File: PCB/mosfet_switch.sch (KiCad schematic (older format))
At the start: 4 parts, among them Q1 DMN1150UFB-7B, Q2 NVTR0202PLT1G

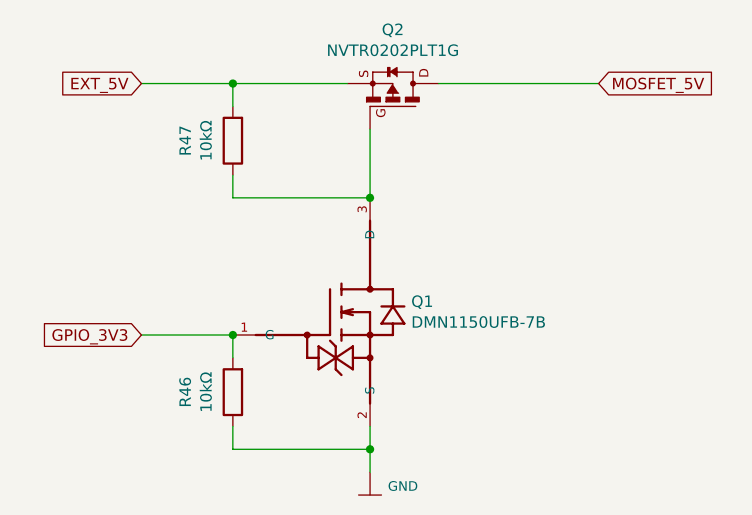
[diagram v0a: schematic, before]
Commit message: Patrick: implemented fuses and bidirectional security diodes for powering lines.
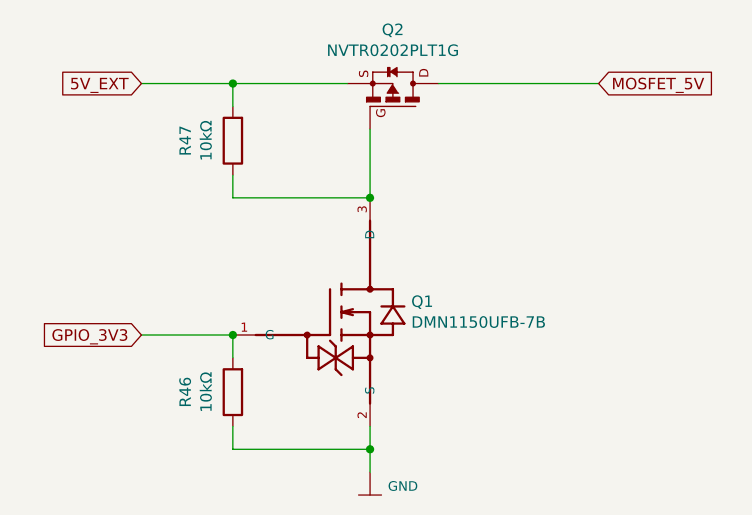
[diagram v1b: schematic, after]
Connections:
- net EXT_5V renamed 5V_EXT
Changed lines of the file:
@@
 MOSFET_5V
 Text GLabel 5000 2900 0    50   Input ~ 0
-EXT_5V
+5V_EXT
 $Comp
 L DMN1150UFB-7B:DMN1150UFB-7B Q1

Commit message: Patrick: added jumper to bridge the two individual external power lines, improved grounding.
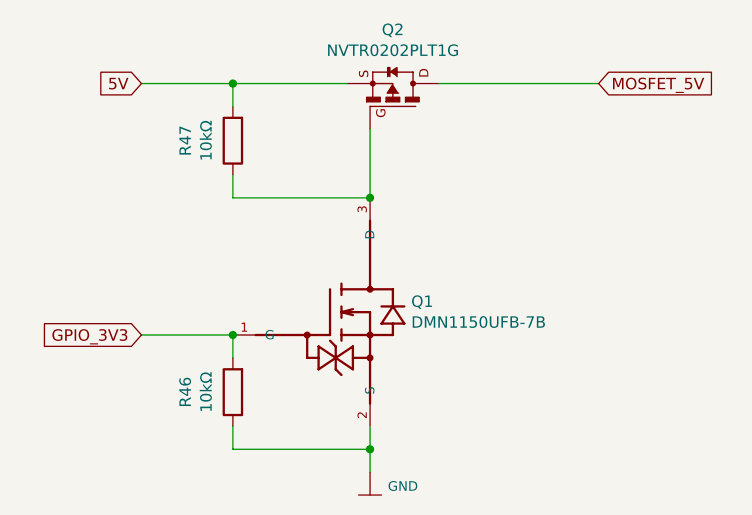
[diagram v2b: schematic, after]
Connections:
- net 5V_EXT renamed 5V
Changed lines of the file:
@@
 EESchema Schematic File Version 4
-LIBS:ArgonCubeSlowControl-cache
-EELAYER 26 0
+EELAYER 30 0
 EELAYER END
 $Descr User 12143 8268
@@
 MOSFET_5V
 Text GLabel 5000 2900 0    50   Input ~ 0
-5V_EXT
+5V
 $Comp
 L DMN1150UFB-7B:DMN1150UFB-7B Q1

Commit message: Patrick: Cosmetics.
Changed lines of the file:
@@
 $EndComp
-Wire Wire Line
-	6000 4500 6000 4400
 Wire Wire Line
 	5400 4000 5400 4100
@@
 Wire Wire Line
 	6000 4500 6000 4600
-Connection ~ 6000 4500
 $Comp
 L Adafruit_MAX31865-eagle-import:GND #0111
@@
 Wire Wire Line
 	6300 2900 7000 2900
+Wire Wire Line
+	6000 4400 6000 4500
+Connection ~ 6000 4500
 $EndSCHEMATC
